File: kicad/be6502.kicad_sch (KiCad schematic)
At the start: 0 parts

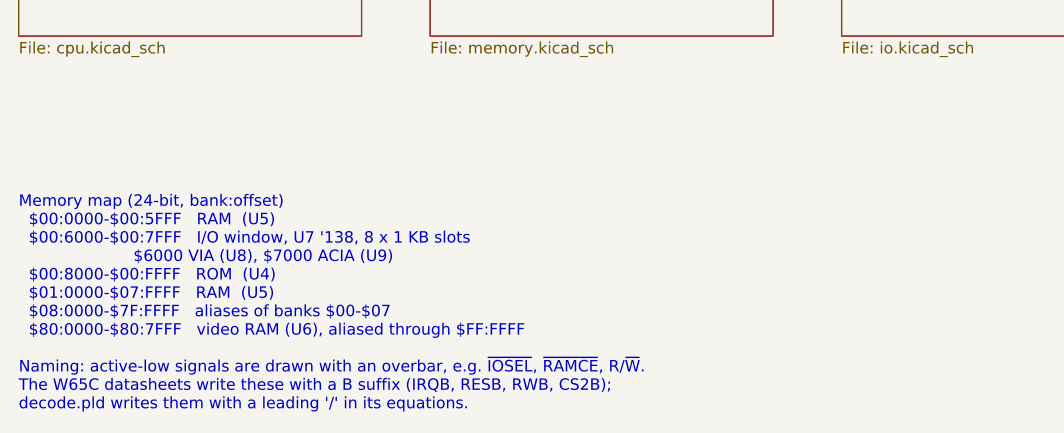
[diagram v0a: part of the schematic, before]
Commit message: Update KiCad schematic to match the build as wired
- Remove video RAM (future expansion); GAL ~{VRAMCE} is NC and
  ~{WEGATE} goes only to the RAM
- VIA is a W65C22N6TPG-14: IRQB wired directly to ~{IRQ} (no diode)
- RDY and ~{NMI} tied directly to +5V; only reset and ~{IRQ} pull-ups
- ACIA clocked by a 1.8432 MHz DIP-8 oscillator on XTLI (EN high)
- Serial through a MAX232N to a female DB9 (pins 2, 3, 8, 5)
- VIA Port B drives eight LEDs with series resistors; Port A, CA/CB NC
- Drop per-chip decoupling; single 0.1uF electrolytic at the supply
- Unknown resistor values shown as '?'
- Update kicad/README.md and README.md accordingly

Co-Authored-By: Claude Opus 5.5 <noreply@anthropic.com>
Claude-Session: https://claude.ai/code/session_01GgTWzZQQJPzWrEMiSDZH6j
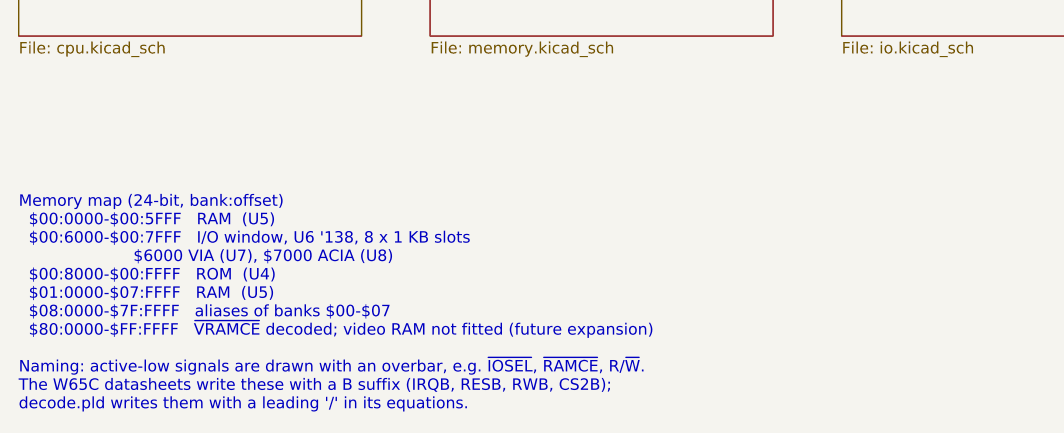
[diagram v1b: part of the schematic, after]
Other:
- note added: "Memory map (24-bit, bank:offset) $00:0000-$00:5FFF RAM (U5) $00:6000-$00:7FFF I/O window, U6 '138, 8 x 1 KB slots $6000 VIA (U7), $7000 ACIA (U8) $00:8000-$00:FFFF ROM (U4) $01:0000-$07:FFFF RAM (U5) $08:0000-$7F:FFFF aliases of banks $00-$07 $80:0000-$FF:FFFF ~{VRAMCE} decoded; video RAM not fitted (future expansion) Naming: active-low signals are drawn with an overbar, e.g. ~{IOSEL}, ~{RAMCE}, 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"
- note removed: "Memory map (24-bit, bank:offset) $00:0000-$00:5FFF RAM (U5) $00:6000-$00:7FFF I/O window, U7 '138, 8 x 1 KB slots $6000 VIA (U8), $7000 ACIA (U9) $00:8000-$00:FFFF ROM (U4) $01:0000-$07:FFFF RAM (U5) $08:0000-$7F:FFFF aliases of banks $00-$07 $80:0000-$80:7FFF video RAM (U6), aliased through $FF:FFFF Naming: active-low signals are drawn with an overbar, e.g. ~{IOSEL}, ~{RAMCE}, R/~{W}. The W65C d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"
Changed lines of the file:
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@@
 (paper "A4")
 (title_block (title "be6502 - W65C816S breadboard computer") (date "2026-10-16") (rev "1") (company "be6502") (comment 1 "W65C816S breadboard computer - see README.md and pld/decode.pld") (comment 2 "Active-low signals use KiCad overbar notation, e.g. ~{IOSEL}"))
-(text "Memory map (24-bit, bank:offset)\n  $00:0000-$00:5FFF   RAM  (U5)\n  $00:6000-$00:7FFF   I/O window, U7 '138, 8 x 1 KB slots\n                       $6000 VIA (U8), $7000 ACIA (U9)\n  $00:8000-$00:FFFF   ROM  (U4)\n  $01:0000-$07:FFFF   RAM  (U5)\n  $08:0000-$7F:FFFF   aliases of banks $00-$07\n  $80:0000-$80:7FFF   video RAM (U6), aliased through $FF:FFFF\n\nNaming: active-low signals are drawn with an overbar, e.g. ~{IOSEL}, ~{RAMCE}, R/~{W}.\nThe W65C datasheets write these with a B suffix (IRQB, RESB, RWB, CS2B);\ndecode.pld writes them with a leading '/' in its equations." (at 25.4 76.2 0) (effects (font (size 1.27 1.27)) (justify left top)))
+(text "Memory map (24-bit, bank:offset)\n  $00:0000-$00:5FFF   RAM  (U5)\n  $00:6000-$00:7FFF   I/O window, U6 '138, 8 x 1 KB slots\n                       $6000 VIA (U7), $7000 ACIA (U8)\n  $00:8000-$00:FFFF   ROM  (U4)\n  $01:0000-$07:FFFF   RAM  (U5)\n  $08:0000-$7F:FFFF   aliases of banks $00-$07\n  $80:0000-$FF:FFFF   ~{VRAMCE} decoded; video RAM not fitted (future expansion)\n\nNaming: active-low signals are drawn with an overbar, e.g. ~{IOSEL}, ~{RAMCE}, R/~{W}.\nThe W65C datasheets write these with a B suffix (IRQB, RESB, RWB, CS2B);\ndecode.pld writes them with a leading '/' in its equations." (at 25.4 76.2 0) (effects (font (size 1.27 1.27)) (justify left top)))
 (sheet (at 25.4 38.1) (size 38.1 20.32) (fields_autoplaced) (stroke (width 0.1524) (type solid)) (fill (color 0 0 0 0.0000)) (property "Sheetname" "CPU and decode" (at 25.4 37.4 0) (effects (font (size 1.27 1.27)) (justify left bottom))) (property "Sheetfile" "cpu.kicad_sch" (at 25.4 59.02 0) (effects (font (size 1.27 1.27)) (justify left top))) (instances (project "be6502" (path "/c8451a90-6bbf-595d-a4c9-ea2cdd0996a1" (page "2")))))
 (sheet (at 71.12 38.1) (size 38.1 20.32) (fields_autoplaced) (stroke (width 0.1524) (type solid)) (fill (color 0 0 0 0.0000)) (property "Sheetname" "Memory" (at 71.12 37.4 0) (effects (font (size 1.27 1.27)) (justify left bottom))) (property "Sheetfile" "memory.kicad_sch" (at 71.12 59.02 0) (effects (font (size 1.27 1.27)) (justify left top))) (instances (project "be6502" (path "/c8451a90-6bbf-595d-a4c9-ea2cdd0996a1" (page "3")))))

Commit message: Schematic rev 2: prepare the design for a 4-layer PCB
Keeps the breadboard's parts and logic and adds what a board needs.

- RDY, NMI, ABORT and BE get 3.3k pull-ups instead of hard ties to +5V
  (RDY is bidirectional; WAI drives it low).
- VDA and VPA go to GAL pins 11 and 13. New pld/decode03.pld (816DEC03)
  qualifies /IOSEL with VDA + VPA so internal-operation cycles cannot
  read and clear ACIA/VIA registers. decode.pld (816DEC02) stays for the
  breadboard.
- PHI2 from the GAL can be routed through a 74ACT08 buffer via JP2
  (default: direct, as built). Timing in decode03.pld NOTE 8.
- Clock source jumper JP1 and external clock header J5.
- New power sheet: USB-C (power only) or bench terminal via JP4, power
  switch, polyfuse, P-FET reverse-polarity protection, 47uF bulk, power
  LED, and 100nF decoupling per package.
- New expansion sheet: 2x30 bus header (address, latched bank byte,
  data, control, spare I/O slots), 2x12 VIA header, LED disconnect
  jumper, test points, mounting holes.
- Footprints on every part; socket footprints for all ICs.

ERC (KiCad 9.0.4 kicad-cli): 0 errors, 0 warnings. Both PLD files
assemble with Galette 0.3.0.

Co-Authored-By: Claude Opus 5.5 <noreply@anthropic.com>
Claude-Session: https://claude.ai/code/session_01WF6ESyzfg6uQED2DRD2W4Z
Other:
- added sheet Expansion and debug (expansion.kicad_sch)
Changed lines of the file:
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@@
 (kicad_sch (version 20230121) (generator eeschema)
 (paper "A4")
-(title_block (title "be6502 - W65C816S breadboard computer") (date "2026-10-16") (rev "1") (company "be6502") (comment 1 "W65C816S breadboard computer - see README.md and pld/decode.pld") (comment 2 "Active-low signals use KiCad overbar notation, e.g. ~{IOSEL}"))
+(title_block (title "be6502 - W65C816S breadboard computer") (date "2026-10-16") (rev "2") (company "be6502") (comment 1 "W65C816S breadboard computer - see README.md and pld/decode.pld") (comment 2 "Active-low signals use KiCad overbar notation, e.g. ~{IOSEL}"))
 (text "Memory map (24-bit, bank:offset)\n  $00:0000-$00:5FFF   RAM  (U5)\n  $00:6000-$00:7FFF   I/O window, U6 '138, 8 x 1 KB slots\n                       $6000 VIA (U7), $7000 ACIA (U8)\n  $00:8000-$00:FFFF   ROM  (U4)\n  $01:0000-$07:FFFF   RAM  (U5)\n  $08:0000-$7F:FFFF   aliases of banks $00-$07\n  $80:0000-$FF:FFFF   ~{VRAMCE} decoded; video RAM not fitted (future expansion)\n\nNaming: active-low signals are drawn with an overbar, e.g. ~{IOSEL}, ~{RAMCE}, R/~{W}.\nThe W65C datasheets write these with a B suffix (IRQB, RESB, RWB, CS2B);\ndecode.pld writes them with a leading '/' in its equations." (at 25.4 76.2 0) (effects (font (size 1.27 1.27)) (justify left top)))
 (sheet (at 25.4 38.1) (size 38.1 20.32) (fields_autoplaced) (stroke (width 0.1524) (type solid)) (fill (color 0 0 0 0.0000)) (property "Sheetname" "CPU and decode" (at 25.4 37.4 0) (effects (font (size 1.27 1.27)) (justify left bottom))) (property "Sheetfile" "cpu.kicad_sch" (at 25.4 59.02 0) (effects (font (size 1.27 1.27)) (justify left top))) (instances (project "be6502" (path "/c8451a90-6bbf-595d-a4c9-ea2cdd0996a1" (page "2")))))
@@
 (sheet (at 116.84 38.1) (size 38.1 20.32) (fields_autoplaced) (stroke (width 0.1524) (type solid)) (fill (color 0 0 0 0.0000)) (property "Sheetname" "I/O" (at 116.84 37.4 0) (effects (font (size 1.27 1.27)) (justify left bottom))) (property "Sheetfile" "io.kicad_sch" (at 116.84 59.02 0) (effects (font (size 1.27 1.27)) (justify left top))) (instances (project "be6502" (path "/c8451a90-6bbf-595d-a4c9-ea2cdd0996a1" (page "4")))))
 (sheet (at 162.56 38.1) (size 38.1 20.32) (fields_autoplaced) (stroke (width 0.1524) (type solid)) (fill (color 0 0 0 0.0000)) (property "Sheetname" "Power" (at 162.56 37.4 0) (effects (font (size 1.27 1.27)) (justify left bottom))) (property "Sheetfile" "power.kicad_sch" (at 162.56 59.02 0) (effects (font (size 1.27 1.27)) (justify left top))) (instances (project "be6502" (path "/c8451a90-6bbf-595d-a4c9-ea2cdd0996a1" (page "5")))))
+(sheet (at 208.28 38.1) (size 38.1 20.32) (fields_autoplaced) (stroke (width 0.1524) (type solid)) (fill (color 0 0 0 0.0000)) (property "Sheetname" "Expansion and debug" (at 208.28 37.4 0) (effects (font (size 1.27 1.27)) (justify left bottom))) (property "Sheetfile" "expansion.kicad_sch" (at 208.28 59.02 0) (effects (font (size 1.27 1.27)) (justify left top))) (instances (project "be6502" (path "/c8451a90-6bbf-595d-a4c9-ea2cdd0996a1" (page "6")))))
 (sheet_instances (path "/" (page "1")))
 )
